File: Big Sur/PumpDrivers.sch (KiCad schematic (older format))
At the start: 6 parts

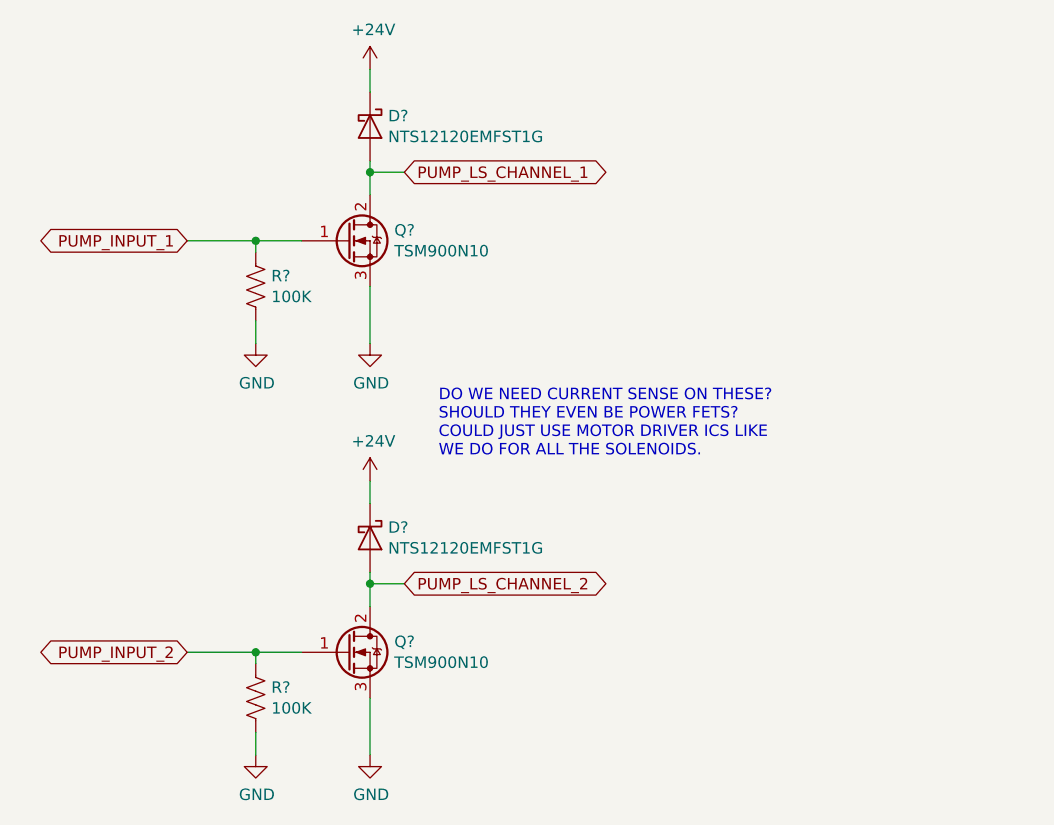
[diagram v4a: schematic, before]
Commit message: Schematics Complete
Still need to spec resistors, and XT30s, then should be ready for layout and routing.
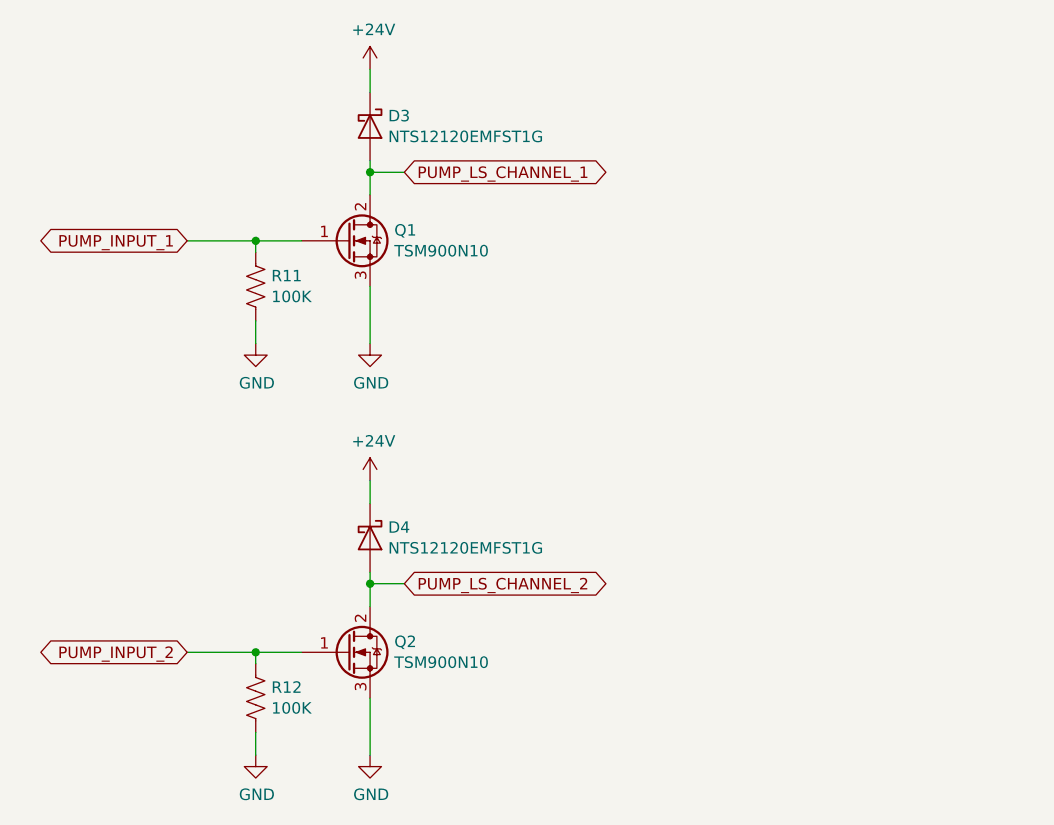
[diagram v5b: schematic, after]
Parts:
- D3, D4: renamed from D?; footprint (none) -> Big Sur:ONSemi_SMD_Schottky_NTS12120EMFS
- Q1, Q2: renamed from Q?; footprint (none) -> Package_TO_SOT_SMD:TO-252-2
- R11, R12: renamed from R?; footprint (none) -> Resistor_SMD:R_0603_1608Metric_Pad1.05x0.95mm_HandSolder
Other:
- note removed: "DO WE NEED CURRENT SENSE ON THESE?\nSHOULD THEY EVEN BE POWER FETS?\nCOULD JUST USE MOTOR DRIVER ICS LIKE\nWE DO FOR ALL THE SOLENOIDS."
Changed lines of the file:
@@
 $EndDescr
 $Comp
-L Device:Q_NMOS_GDS Q?
+L Device:Q_NMOS_GDS Q1
 U 1 1 5D7D3E10
 P 2400 1900
-F 0 "Q?" H 2606 1946 50  0000 L CNN
+F 0 "Q1" H 2606 1946 50  0000 L CNN
 F 1 "TSM900N10" H 2606 1855 50  0000 L CNN
-F 2 "" H 2600 2000 50  0001 C CNN
+F 2 "Package_TO_SOT_SMD:TO-252-2" H 2600 2000 50  0001 C CNN
 F 3 "https://www.taiwansemi.com/products/datasheet/TSM900N10_A15.pdf" H 2400 1900 50  0001 C CNN
 F 4 "https://www.digikey.ca/product-detail/en/taiwan-semiconductor-corporation/TSM900N10CP-ROG/TSM900N10CPROGCT-ND/7360607" H 2400 1900 50  0001 C CNN "Digikey"
@@
 	2500 2100 2500 2350
 $Comp
-L power:GND #PWR?
+L power:GND #PWR042
 U 1 1 5D7D4C28
 P 2500 2350
-F 0 "#PWR?" H 2500 2100 50  0001 C CNN
+F 0 "#PWR042" H 2500 2100 50  0001 C CNN
 F 1 "GND" H 2505 2177 50  0000 C CNN
 F 2 "" H 2500 2350 50  0001 C CNN
@@
 	2000 1900 1700 1900
 $Comp
-L Device:R_US R?
+L Device:R_US R11
 U 1 1 5D7D75FE
 P 2000 2100
-F 0 "R?" H 2068 2146 50  0000 L CNN
+F 0 "R11" H 2068 2146 50  0000 L CNN
 F 1 "100K" H 2068 2055 50  0000 L CNN
-F 2 "" V 2040 2090 50  0001 C CNN
+F 2 "Resistor_SMD:R_0603_1608Metric_Pad1.05x0.95mm_HandSolder" V 2040 2090 50  0001 C CNN
 F 3 "~" H 2000 2100 50  0001 C CNN
 	1    2000 2100
@@
 $EndComp
 $Comp
-L power:GND #PWR?
+L power:GND #PWR041
 U 1 1 5D7D85EE
 P 2000 2350
-F 0 "#PWR?" H 2000 2100 50  0001 C CNN
+F 0 "#PWR041" H 2000 2100 50  0001 C CNN
 F 1 "GND" H 2005 2177 50  0000 C CNN
 F 2 "" H 2000 2350 50  0001 C CNN
@@
 	2500 1550 2500 1600
 $Comp
-L power:+24V #PWR?
+L power:+24V #PWR040
 U 1 1 5D6DC51E
 P 2500 1150
-F 0 "#PWR?" H 2500 1000 50  0001 C CNN
+F 0 "#PWR040" H 2500 1000 50  0001 C CNN
 F 1 "+24V" H 2515 1323 50  0000 C CNN
 F 2 "" H 2500 1150 50  0001 C CNN
@@
 $EndComp
 $Comp
-L Device:D_Schottky D?
+L Device:D_Schottky D3
 U 1 1 5D6DD7E1
 P 2500 1400
-F 0 "D?" V 2454 1479 50  0000 L CNN
+F 0 "D3" V 2454 1479 50  0000 L CNN
 F 1 "NTS12120EMFST1G" V 2545 1479 50  0000 L CNN
-F 2 "" H 2500 1400 50  0001 C CNN
+F 2 "Big Sur:ONSemi_SMD_Schottky_NTS12120EMFS" H 2500 1400 50  0001 C CNN
 F 3 "https://www.onsemi.com/pub/Collateral/NTS12120EMFS-D.PDF" H 2500 1400 50  0001 C CNN
 F 4 "https://www.digikey.ca/product-detail/en/on-semiconductor/NTS12120EMFST1G/NTS12120EMFST1GOSCT-ND/8538813" V 2500 1400 50  0001 C CNN "Digikey"
@@
 PUMP_INPUT_1
 $Comp
-L Device:Q_NMOS_GDS Q?
+L Device:Q_NMOS_GDS Q2
 U 1 1 5D85B099
 P 2400 3700
-F 0 "Q?" H 2606 3746 50  0000 L CNN
+F 0 "Q2" H 2606 3746 50  0000 L CNN
 F 1 "TSM900N10" H 2606 3655 50  0000 L CNN
-F 2 "" H 2600 3800 50  0001 C CNN
+F 2 "Package_TO_SOT_SMD:TO-252-2" H 2600 3800 50  0001 C CNN
 F 3 "https://www.taiwansemi.com/products/datasheet/TSM900N10_A15.pdf" H 2400 3700 50  0001 C CNN
 F 4 "https://www.digikey.ca/product-detail/en/taiwan-semiconductor-corporation/TSM900N10CP-ROG/TSM900N10CPROGCT-ND/7360607" H 2400 3700 50  0001 C CNN "Digikey"
@@
 	2500 3900 2500 4150
 $Comp
-L power:GND #PWR?
+L power:GND #PWR045
 U 1 1 5D85B0A4
 P 2500 4150
-F 0 "#PWR?" H 2500 3900 50  0001 C CNN
+F 0 "#PWR045" H 2500 3900 50  0001 C CNN
 F 1 "GND" H 2505 3977 50  0000 C CNN
 F 2 "" H 2500 4150 50  0001 C CNN
@@
 	2000 3700 1700 3700
 $Comp
-L Device:R_US R?
+L Device:R_US R12
 U 1 1 5D85B0B6
 P 2000 3900
-F 0 "R?" H 2068 3946 50  0000 L CNN
+F 0 "R12" H 2068 3946 50  0000 L CNN
 F 1 "100K" H 2068 3855 50  0000 L CNN
-F 2 "" V 2040 3890 50  0001 C CNN
+F 2 "Resistor_SMD:R_0603_1608Metric_Pad1.05x0.95mm_HandSolder" V 2040 3890 50  0001 C CNN
 F 3 "~" H 2000 3900 50  0001 C CNN
 	1    2000 3900
@@
 $EndComp
 $Comp
-L power:GND #PWR?
+L power:GND #PWR044
 U 1 1 5D85B0C0
 P 2000 4150
-F 0 "#PWR?" H 2000 3900 50  0001 C CNN
+F 0 "#PWR044" H 2000 3900 50  0001 C CNN
 F 1 "GND" H 2005 3977 50  0000 C CNN
 F 2 "" H 2000 4150 50  0001 C CNN
@@
 	2500 3350 2500 3400
 $Comp
-L power:+24V #PWR?
+L power:+24V #PWR043
 U 1 1 5D85B0CC
 P 2500 2950
-F 0 "#PWR?" H 2500 2800 50  0001 C CNN
+F 0 "#PWR043" H 2500 2800 50  0001 C CNN
 F 1 "+24V" H 2515 3123 50  0000 C CNN
 F 2 "" H 2500 2950 50  0001 C CNN
@@
 $EndComp
 $Comp
-L Device:D_Schottky D?
+L Device:D_Schottky D4
 U 1 1 5D85B0D7
 P 2500 3200
-F 0 "D?" V 2454 3279 50  0000 L CNN
+F 0 "D4" V 2454 3279 50  0000 L CNN
 F 1 "NTS12120EMFST1G" V 2545 3279 50  0000 L CNN
-F 2 "" H 2500 3200 50  0001 C CNN
+F 2 "Big Sur:ONSemi_SMD_Schottky_NTS12120EMFS" H 2500 3200 50  0001 C CNN
 F 3 "https://www.onsemi.com/pub/Collateral/NTS12120EMFS-D.PDF" H 2500 3200 50  0001 C CNN
 F 4 "https://www.digikey.ca/product-detail/en/on-semiconductor/NTS12120EMFST1G/NTS12120EMFST1GOSCT-ND/8538813" V 2500 3200 50  0001 C CNN "Digikey"
@@
 Text GLabel 1700 3700 0    50   BiDi ~ 0
 PUMP_INPUT_2
-Text Notes 2800 2850 0    50   ~ 0
-DO WE NEED CURRENT SENSE ON THESE?\nSHOULD THEY EVEN BE POWER FETS?\nCOULD JUST USE MOTOR DRIVER ICS LIKE\nWE DO FOR ALL THE SOLENOIDS.
 $EndSCHEMATC
